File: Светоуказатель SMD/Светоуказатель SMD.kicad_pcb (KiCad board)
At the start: 2 copper layers, 64 parts, among them J2 Отладка SWD, J3 Питание БС, J4 Земля БС, J5 +Пит. панель, J6 -Пит. панель, J7 Линия 1, J8 Линия 2, J9 RS232 Выходы, Q1 S8550, Q2 S8550, SW1 SW_Push, U1 TPS5430DDA, U2 AMS1117-3.3, U3 STM32F103C8Tx, U4 MAX3232, U5 ADuM1201AR, Y1 8 МГц

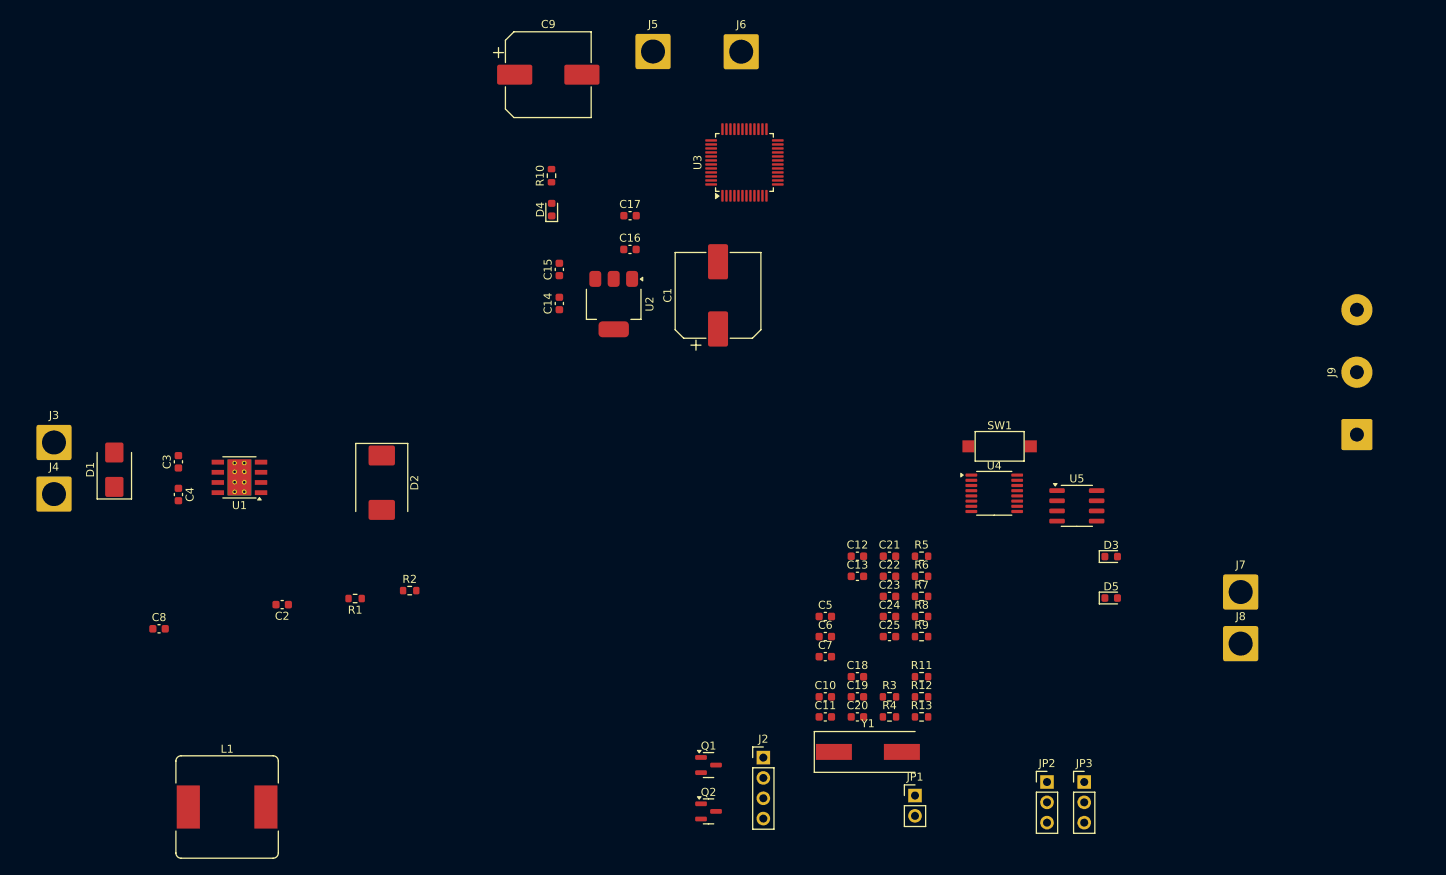
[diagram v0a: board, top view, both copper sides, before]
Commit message: Add some routing
Add net routing for input power and DC/DC 3.3v.
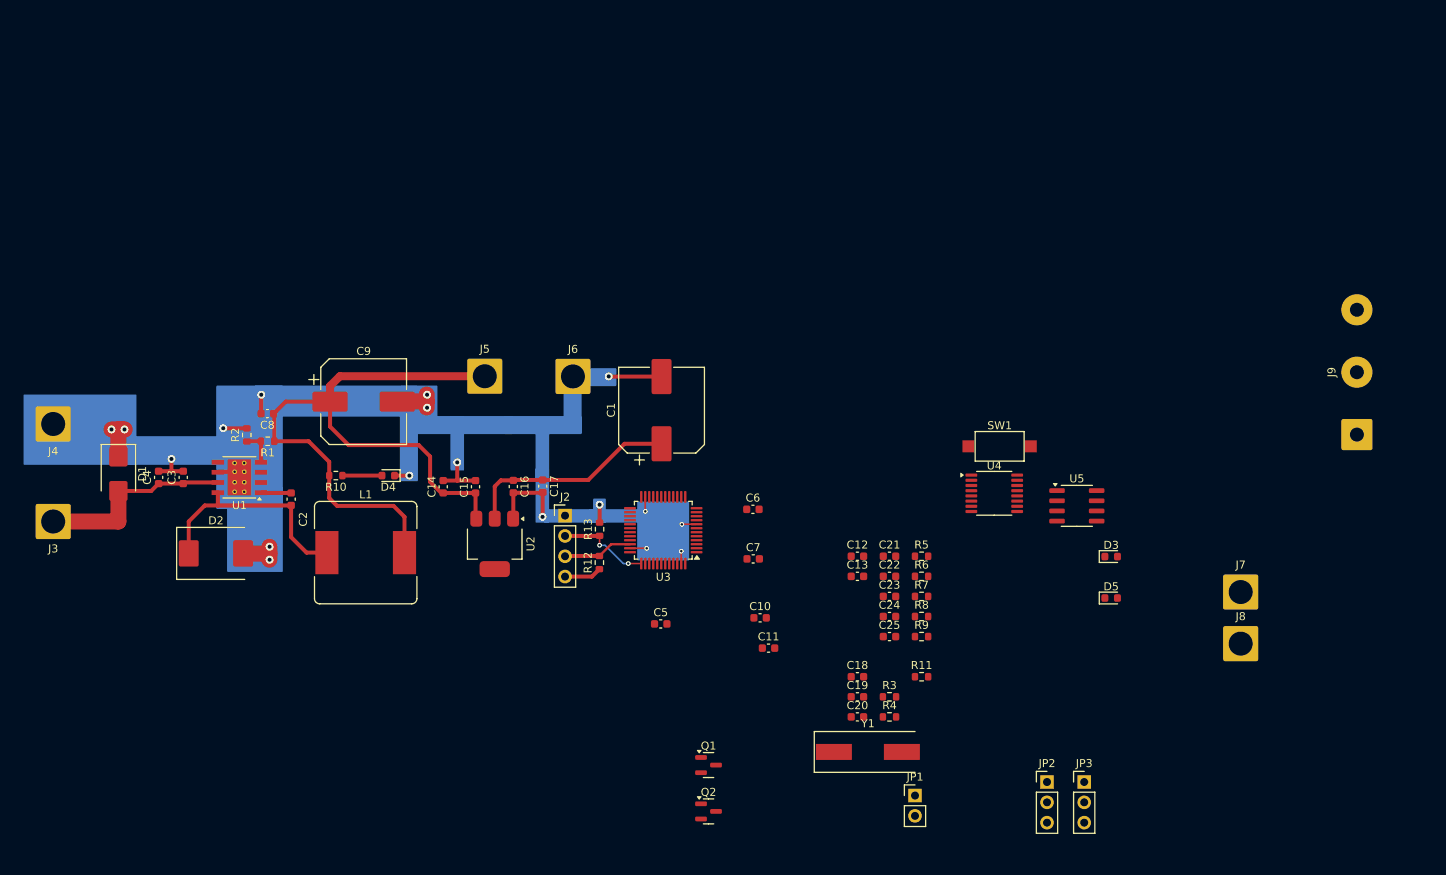
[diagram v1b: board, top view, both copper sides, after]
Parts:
- moved U3 47.1 mm to (124.1, 97.7), turned to 180 degrees
- moved C9 46.9 mm to (86.7, 81.6)
- moved R13 46.6 mm to (116.2, 97.6), turned to 90 degrees
- moved R10 46.2 mm to (83.2, 90.9), turned to 180 degrees
- moved J5 45.7 mm to (101.8, 78.4)
- moved J6 45.7 mm to (112.8, 78.5)
- moved R12 43.6 mm to (116.1, 101.7), turned to 90 degrees
- moved J2 39.1 mm to (111.8, 95.9)
- moved D4 39.0 mm to (89.7, 90.9), turned to 180 degrees
- moved L1 36.2 mm to (86.9, 100.5)
- moved C17 35.5 mm to (109.1, 92.2), turned to -90 degrees
- moved U2 33.5 mm to (103.0, 99.4)
- moved C16 33.0 mm to (105.4, 92.2), turned to -90 degrees
- moved C8 30.1 mm to (74.6, 83.1), turned to 180 degrees
- moved C15 29.1 mm to (100.6, 92.3)
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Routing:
- net +5В: track 0.00 -> 89.8 mm
- net GND: track 0.00 -> 62.4 mm, vias 0 -> 18
- net +3.3В: track 0.00 -> 31.8 mm
- net Net-(D2-K): track 0.00 -> 28.5 mm
- net VIN: track 0.00 -> 24.8 mm
- net /SWCLK: track 0.00 -> 11.7 mm, vias 0 -> 2
- net /SWDIO: track 0.00 -> 8.74 mm
- net Net-(D4-A): track 0.00 -> 4.94 mm
- net Net-(U1-VSENSE): track 0.00 -> 4.42 mm
- net Net-(U1-BOOT): track 0.00 -> 3.72 mm

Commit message: MCU net routing.
Add MCU routing to project.
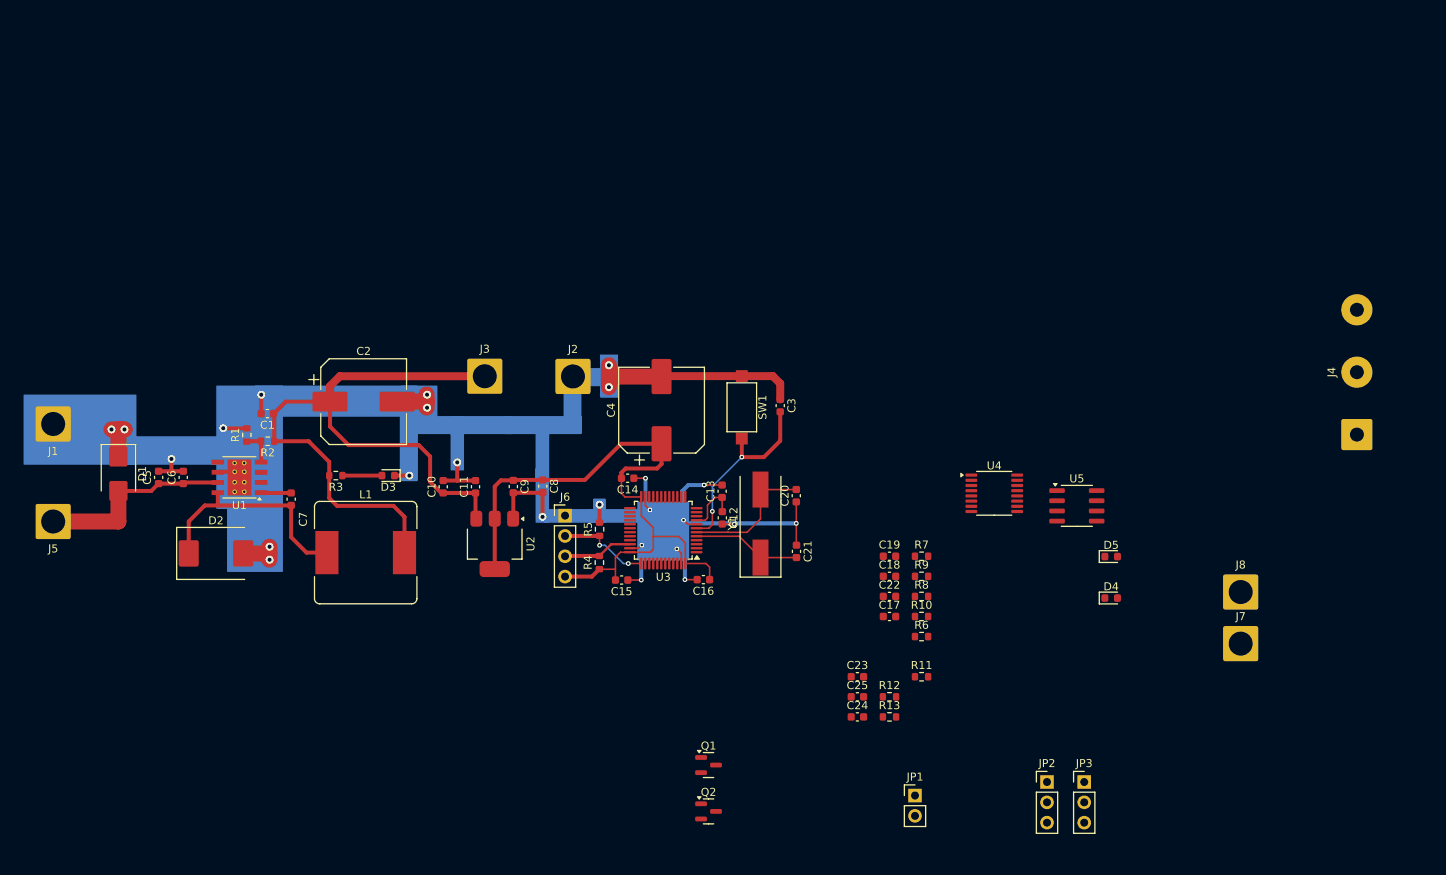
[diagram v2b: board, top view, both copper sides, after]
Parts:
- moved SW1 32.6 mm to (133.9, 82.3), turned to -90 degrees
- moved C3 31.9 mm to (138.7, 82.1), turned to -90 degrees
- moved Y1 31.5 mm to (136.3, 96.9), turned to 90 degrees
- moved C13 20.4 mm to (131.5, 92.8), turned to 90 degrees
- moved C14 16.1 mm to (119.7, 91.2), turned to 180 degrees
- moved C12 13.4 mm to (131.5, 96.1), turned to -90 degrees
- moved C20 12.6 mm to (140.7, 93.4), turned to 90 degrees
- moved C21 7.64 mm to (140.8, 100.3), turned to -90 degrees
- moved C15 7.35 mm to (118.9, 103.9), turned to 180 degrees
- moved C16 6.74 mm to (129.1, 103.9), turned to 180 degrees
- renumbered C8 to C1, C14 to C10, C15 to C11, C10 to C12, C11 to C13, C6 to C14, C5 to C15, C7 to C16, C24 to C17, C22 to C18, C21 to C19, C9 to C2, C13 to C20, C12 to C21, C23 to C22, C18 to C23, C20 to C24, C19 to C25, C25 to C3, C1 to C4, C4 to C5, C3 to C6, C2 to C7, C17 to C8, C16 to C9, D4 to D3, D5 to D4, D3 to D5, J4 to J1, J6 to J2, J5 to J3, J9 to J4, J3 to J5, J2 to J6, J8 to J7, J7 to J8, R2 to R1, R8 to R10, R3 to R12, R4 to R13, R1 to R2, R10 to R3, R12 to R4, R13 to R5, R9 to R6, R5 to R7, R7 to R8, R6 to R9
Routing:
- net GND: track 62.4 -> 128.7 mm, vias 18 -> 25
- net +3.3В: track 31.8 -> 80.2 mm
- net NRST: track 0.00 -> 23.8 mm, vias 0 -> 2
- net Net-(U3-PD1): track 0.00 -> 16.8 mm
- net Net-(U3-PD0): track 0.00 -> 13.6 mm
- net Net-(U3-VDDA): track 0.00 -> 7.11 mm

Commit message: Add full component places.
Set component places for board without routing.
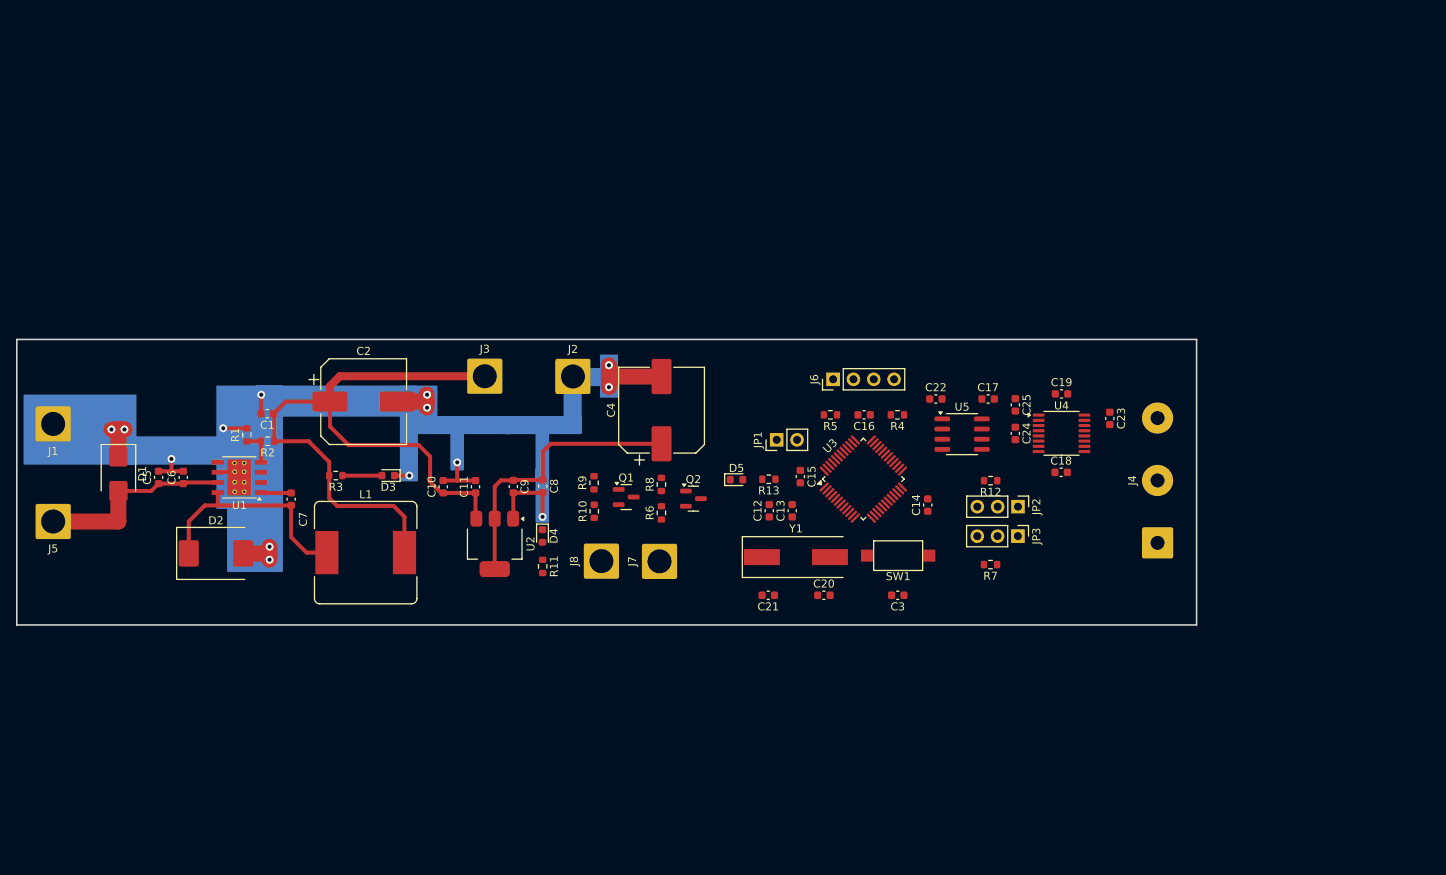
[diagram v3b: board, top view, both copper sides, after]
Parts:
- moved J8 80.0 mm to (116.4, 101.5), turned to 90 degrees
- moved J7 73.4 mm to (123.6, 101.6), turned to 90 degrees
- moved D4 71.5 mm to (109.0, 98.4), turned to -90 degrees
- moved R11 49.3 mm to (109.0, 102.2), turned to -90 degrees
- moved D5 47.8 mm to (133.3, 91.4)
- moved JP1 47.7 mm to (138.3, 86.4), turned to 90 degrees
- moved C23 45.1 mm to (179.9, 83.7), turned to -90 degrees
- moved R10 43.0 mm to (115.5, 95.3), turned to 90 degrees
- moved R9 42.6 mm to (115.5, 91.8), turned to 90 degrees
- moved R4 41.6 mm to (153.4, 83.3), turned to 180 degrees
- moved C25 41.5 mm to (168.1, 82.0), turned to -90 degrees
- moved C24 40.6 mm to (168.1, 85.6), turned to -90 degrees
- moved Q2 39.1 mm to (127.9, 93.7)
- moved C14 37.7 mm to (157.2, 94.5), turned to 90 degrees
- moved J6 37.6 mm to (145.3, 78.8), turned to 90 degrees
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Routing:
- net GND: track 128.7 -> 55.3 mm, vias 25 -> 14
- net +3.3В: track 80.2 -> 35.5 mm
- net NRST: track 23.8 -> 0.00 mm, vias 2 -> 0
- net Net-(U3-PD1): track 16.8 -> 0.00 mm
- net Net-(U3-PD0): track 13.6 -> 0.00 mm
- net /SWCLK: track 11.7 -> 0.00 mm, vias 2 -> 0
- net /SWDIO: track 8.74 -> 0.00 mm
- net Net-(U3-VDDA): track 7.11 -> 0.00 mm
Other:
- board outline added: 147.5 x 35.7 mm

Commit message: Full routing add.
Complete full touting for board.
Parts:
- removed JP1: VBAT_PWR, Connector_PinHeader_2.54mm:PinHeader_1x02_P2.54mm_Vertical
- removed JP2: BOOT0_MODE, Connector_PinHeader_2.54mm:PinHeader_1x03_P2.54mm_Vertical
- removed JP3: BOOT1_MODE, Connector_PinHeader_2.54mm:PinHeader_1x03_P2.54mm_Vertical
- moved J8 45.4 mm to (155.2, 78.0), turned to 0 degrees
- moved R9 36.4 mm to (148.7, 77.0), turned to 180 degrees
- moved R10 34.0 mm to (148.1, 85.6)
- moved Q1 32.0 mm to (148.9, 81.1), turned to 90 degrees
- moved J7 26.9 mm to (136.5, 78.0), turned to 0 degrees
- moved SW1 25.5 mm to (128.0, 100.7), turned to 0 degrees
- moved C3 25.3 mm to (128.2, 103.7), turned to 0 degrees
- moved R8 24.1 mm to (142.8, 77.0), turned to 0 degrees
- moved C22 23.6 mm to (168.4, 102.6), turned to -90 degrees
- moved C20 22.7 mm to (128.7, 89.3), turned to 180 degrees
- moved R6 22.4 mm to (143.9, 85.5)
- moved R7 19.7 mm to (145.8, 106.5), turned to 90 degrees
- moved Q2 19.7 mm to (142.9, 81.1), turned to 90 degrees
- moved C15 18.8 mm to (150.9, 107.1), turned to 180 degrees
- moved U5 18.1 mm to (173.4, 99.3), turned to 90 degrees
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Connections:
- R12 pad 1: Net-(JP2-C) -> +3.3В
- R7 pad 1: Net-(JP3-C) -> +3.3В
- U3 pad 1: Net-(JP1-B) -> unconnected-(U3-VBAT-Pad1)
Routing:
- net GND: track 55.3 -> 176.5 mm, vias 14 -> 34
- net +5В: track 89.8 -> 193.6 mm, vias 0 -> 3
- net +3.3В: track 35.5 -> 134.5 mm, vias 0 -> 2
- net RX232_TxD: track 0.00 -> 29.3 mm, vias 0 -> 2
- net RX232_RxD: track 0.00 -> 28.0 mm
- net Net-(U3-PD1): track 0.00 -> 24.2 mm
- net /RxD: track 0.00 -> 23.5 mm
- net /TxD: track 0.00 -> 18.7 mm
- net NRST: track 0.00 -> 18.2 mm
- net /SWDIO: track 0.00 -> 17.8 mm, vias 0 -> 2
- net Net-(U3-PD0): track 0.00 -> 15.3 mm
- net Net-(J8-Pin_1): track 0.00 -> 15.1 mm
- net Net-(U4-R1OUT): track 0.00 -> 14.0 mm, vias 0 -> 2
- net Net-(U3-PC13): track 0.00 -> 13.9 mm
- net Net-(U4-T1IN): track 0.00 -> 13.8 mm, vias 0 -> 2
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
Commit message: Final Design for Board.
All design done.
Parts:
- moved C12 29.4 mm to (169.1, 106.2)
- moved C14 29.4 mm to (174.1, 95.0)
- moved C21 29.4 mm to (164.6, 94.1)
- moved C25 29.4 mm to (198.8, 96.7)
- moved J4 29.4 mm to (214.2, 89.1)
- moved R13 29.4 mm to (168.0, 90.0)
- moved R6 29.4 mm to (172.9, 90.4)
- moved R8 29.4 mm to (171.8, 81.8)
- moved U2 29.4 mm to (132.1, 104.2)
- moved U3 29.4 mm to (176.9, 103.4)
- moved C16 29.4 mm to (184.4, 100.4)
- moved C18 29.4 mm to (207.4, 90.7)
- moved C4 29.4 mm to (146.3, 98.4)
- moved R12 29.4 mm to (178.7, 95.1)
- moved SW1 29.4 mm to (157.0, 105.5)
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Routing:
- net +3.3В: track 134.5 -> 147.3 mm
- net GND: track 176.5 -> 177.8 mm, vias 34 -> 33
- added copper zone on B.Cu, net GND

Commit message: Cap moved.
Move cap from electro to tantal.
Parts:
- C2, C4: footprint Capacitor_SMD:CP_Elec_10x10.5 -> Capacitor_Tantalum_SMD:CP_EIA-7343-43_Kemet-X_Pad2.25x2.55mm_HandSolder
